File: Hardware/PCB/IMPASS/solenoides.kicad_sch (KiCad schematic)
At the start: 7 parts, among them J11 SOLENOIDES, Q43 DMN3008SFG, Q44 DMN3008SFG, Q45 DMN3008SFG

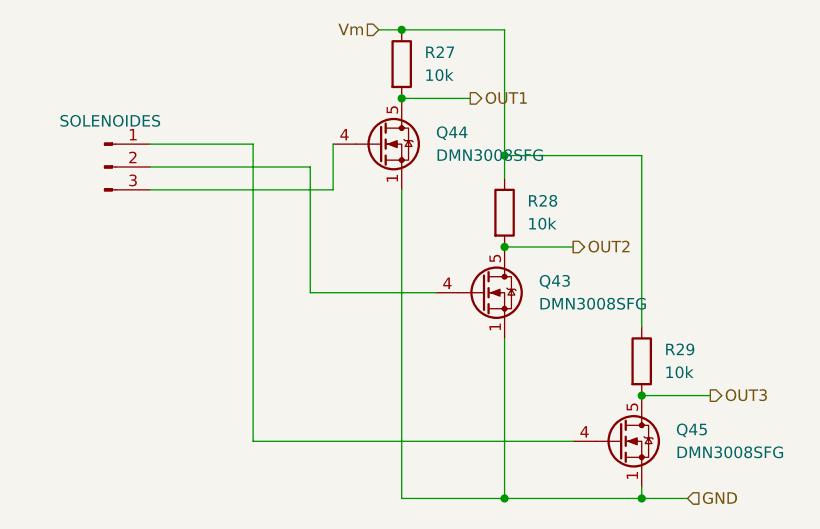
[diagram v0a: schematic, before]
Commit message: Restore all the schematics
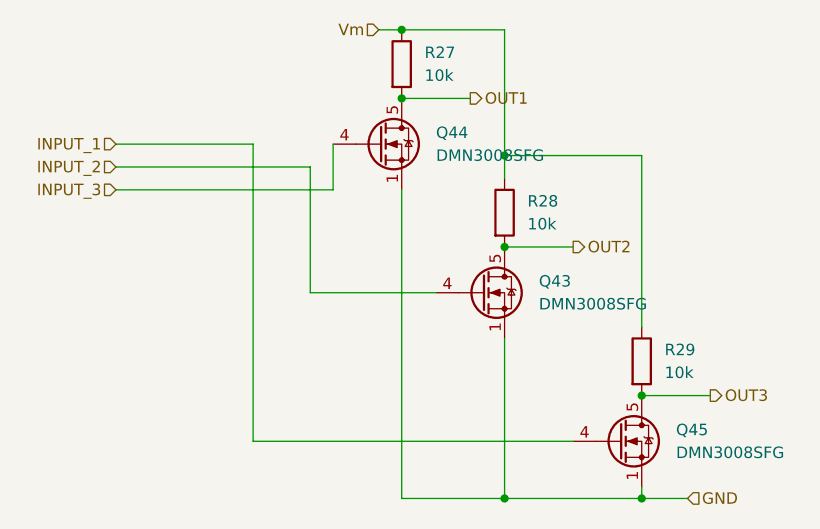
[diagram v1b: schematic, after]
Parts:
- removed J11: SOLENOIDES, Connector_PinHeader_2.54mm:PinHeader_1x03_P2.54mm_Vertical, symbol Connector:Conn_01x03_Pin
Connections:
- net INPUT_1: now reaches Q45.4 (G)
- net INPUT_2: now reaches Q43.4 (G)
- net INPUT_3: now reaches Q44.4 (G)
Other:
- company: (none) -> Luis Miguel Carmona Cortés
- title: (none) -> IMPASS 
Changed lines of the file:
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@@
 (kicad_sch
-	(version 20231120)
+	(version 20250114)
 	(generator "eeschema")
-	(generator_version "8.0")
+	(generator_version "9.0")
 	(paper "A4")
+	(title_block
+		(title "IMPASS ")
+		(date "2026-01-31")
+		(rev "v2.0")
+		(company "Luis Miguel Carmona Cortés")
+		(comment 1 "Mosfets de los solenoides")
+	)
 	(junction
 		(at 116.84 49.53)
@@
 	(wire
 		(pts
-			(xy 88.9 57.15) (xy 106.68 57.15)
-		)
-		(stroke
-			(width 0)
-			(type default)
-		)
-	)
-	(wire
-		(pts
-			(xy 88.9 59.69) (xy 109.22 59.69)
-		)
-		(stroke
-			(width 0)
-			(type default)
-		)
-	)
-	(wire
-		(pts
 			(xy 128.27 41.91) (xy 116.84 41.91)
 		)
@@
 	(wire
 		(pts
+			(xy 85.09 57.15) (xy 106.68 57.15)
+		)
+		(stroke
+			(width 0)
+			(type default)
+		)
+	)
+	(wire
+		(pts
+			(xy 85.09 54.61) (xy 100.33 54.61)
+		)
+		(stroke
+			(width 0)
+			(type default)
+		)
+	)
+	(wire
+		(pts
 			(xy 128.27 66.04) (xy 135.89 66.04)
 		)
@@
 	(wire
 		(pts
-			(xy 88.9 54.61) (xy 100.33 54.61)
+			(xy 85.09 59.69) (xy 109.22 59.69)
 		)
 		(stroke
@@
 			(width 0)
 			(type default)
+		)
+	)
+	(hierarchical_label "INPUT_1"
+		(shape input)
+		(at 85.09 54.61 180)
+		(effects
+			(font
+				(size 1.27 1.27)
+			)
+			(justify right)
 		)
 	)
@@
 		)
 	)
+	(hierarchical_label "INPUT_3"
+		(shape input)
+		(at 85.09 59.69 180)
+		(effects
+			(font
+				(size 1.27 1.27)
+			)
+			(justify right)
+		)
+	)
 	(hierarchical_label "Vm"
 		(shape input)
@@
 			)
 			(justify left)
+		)
+	)
+	(hierarchical_label "INPUT_2"
+		(shape input)
+		(at 85.09 57.15 180)
+		(effects
+			(font
+				(size 1.27 1.27)
+			)
+			(justify right)
 		)
 	)
@@
 		(instances
 			(project "IMPASS"
-				(path "/731b3037-3e9a-4423-b2c0-b5bf223d88c2/f88d884c-2e90-4ed2-b40a-13211fa440f1/268b77bf-d124-4d69-b9d8-4316cbc44bd5"
+				(path "/731b3037-3e9a-4423-b2c0-b5bf223d88c2/acd98061-6367-4cb8-aa42-1ec0ef88ad06/8aa8990d-3e6f-44d3-8f78-3b2081a93340"
 					(reference "R29")
-					(unit 1)
-				)
-			)
-		)
-	)
-	(symbol
-		(lib_id "Connector:Conn_01x03_Pin")
-		(at 83.82 57.15 0)
-		(unit 1)
-		(exclude_from_sim no)
-		(in_bom yes)
-		(on_board yes)
-		(dnp no)
-		(fields_autoplaced yes)
-		(property "Reference" "J11"
-			(at 84.455 49.53 0)
-			(effects
-				(font
-					(size 1.27 1.27)
-				)
-				(hide yes)
-			)
-		)
-		(property "Value" "SOLENOIDES"
-			(at 84.455 52.07 0)
-			(effects
-				(font
-					(size 1.27 1.27)
-				)
-			)
-		)
-		(property "Footprint" "Connector_PinHeader_2.54mm:PinHeader_1x03_P2.54mm_Vertical"
-			(at 83.82 57.15 0)
-			(effects
-				(font
-					(size 1.27 1.27)
-				)
-				(hide yes)
-			)
-		)
-		(property "Datasheet" "~"
-			(at 83.82 57.15 0)
-			(effects
-				(font
-					(size 1.27 1.27)
-				)
-				(hide yes)
-			)
-		)
-		(property "Description" "Generic connector, single row, 01x03, script generated"
-			(at 83.82 57.15 0)
-			(effects
-				(font
-					(size 1.27 1.27)
-				)
-				(hide yes)
-			)
-		)
-		(pin "3"
-		)
-		(pin "1"
-		)
-		(pin "2"
-		)
-		(instances
-			(project "IMPASS"
-				(path "/731b3037-3e9a-4423-b2c0-b5bf223d88c2/f88d884c-2e90-4ed2-b40a-13211fa440f1/268b77bf-d124-4d69-b9d8-4316cbc44bd5"
-					(reference "J11")
 					(unit 1)
 				)
@@
 		(instances
 			(project "IMPASS"
-				(path "/731b3037-3e9a-4423-b2c0-b5bf223d88c2/f88d884c-2e90-4ed2-b40a-13211fa440f1/268b77bf-d124-4d69-b9d8-4316cbc44bd5"
+				(path "/731b3037-3e9a-4423-b2c0-b5bf223d88c2/acd98061-6367-4cb8-aa42-1ec0ef88ad06/8aa8990d-3e6f-44d3-8f78-3b2081a93340"
 					(reference "Q43")
 					(unit 1)
@@
 		(instances
 			(project "IMPASS"
-				(path "/731b3037-3e9a-4423-b2c0-b5bf223d88c2/f88d884c-2e90-4ed2-b40a-13211fa440f1/268b77bf-d124-4d69-b9d8-4316cbc44bd5"
+				(path "/731b3037-3e9a-4423-b2c0-b5bf223d88c2/acd98061-6367-4cb8-aa42-1ec0ef88ad06/8aa8990d-3e6f-44d3-8f78-3b2081a93340"
 					(reference "R27")
 					(unit 1)
@@
 		(instances
 			(project "IMPASS"
-				(path "/731b3037-3e9a-4423-b2c0-b5bf223d88c2/f88d884c-2e90-4ed2-b40a-13211fa440f1/268b77bf-d124-4d69-b9d8-4316cbc44bd5"
+				(path "/731b3037-3e9a-4423-b2c0-b5bf223d88c2/acd98061-6367-4cb8-aa42-1ec0ef88ad06/8aa8990d-3e6f-44d3-8f78-3b2081a93340"
 					(reference "Q44")
 					(unit 1)
@@
 		(instances
 			(project "IMPASS"
-				(path "/731b3037-3e9a-4423-b2c0-b5bf223d88c2/f88d884c-2e90-4ed2-b40a-13211fa440f1/268b77bf-d124-4d69-b9d8-4316cbc44bd5"
+				(path "/731b3037-3e9a-4423-b2c0-b5bf223d88c2/acd98061-6367-4cb8-aa42-1ec0ef88ad06/8aa8990d-3e6f-44d3-8f78-3b2081a93340"
 					(reference "Q45")
 					(unit 1)
@@
 		(instances
 			(project "IMPASS"
-				(path "/731b3037-3e9a-4423-b2c0-b5bf223d88c2/f88d884c-2e90-4ed2-b40a-13211fa440f1/268b77bf-d124-4d69-b9d8-4316cbc44bd5"
+				(path "/731b3037-3e9a-4423-b2c0-b5bf223d88c2/acd98061-6367-4cb8-aa42-1ec0ef88ad06/8aa8990d-3e6f-44d3-8f78-3b2081a93340"
 					(reference "R28")
 					(unit 1)
